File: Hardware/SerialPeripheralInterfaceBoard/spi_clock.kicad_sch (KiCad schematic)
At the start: 5 parts, among them J3 SPI_CLOCK_SPD, U10 74HC161, U2 74HC74, U3 74HC02

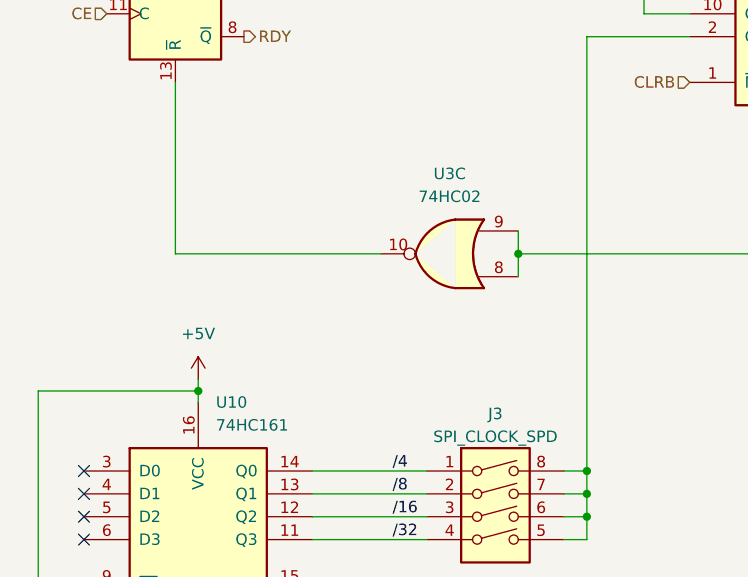
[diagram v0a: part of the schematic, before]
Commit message: feat: modify mother board for paging and dma
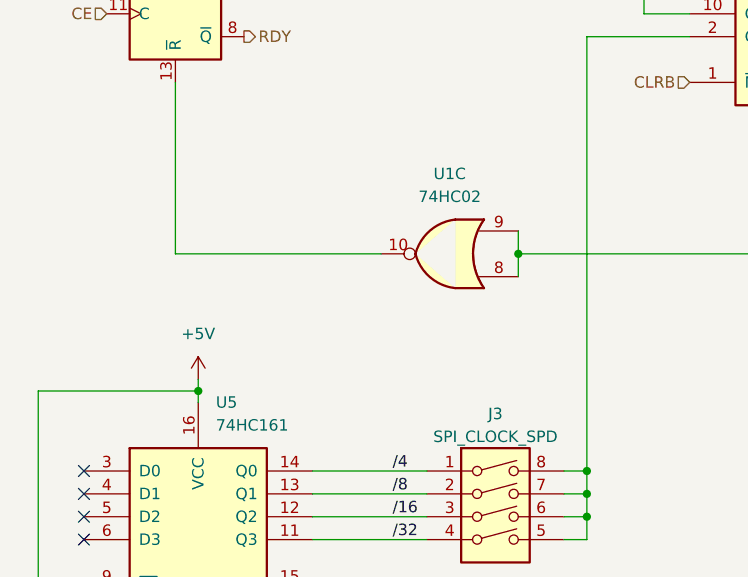
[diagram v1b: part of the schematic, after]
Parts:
- renumbered U3 to U1, U10 to U5
